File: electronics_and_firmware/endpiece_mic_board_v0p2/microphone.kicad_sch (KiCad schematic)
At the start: 7 parts, among them J1 I2S_MIC_EXT, U1 SPH0645LMH

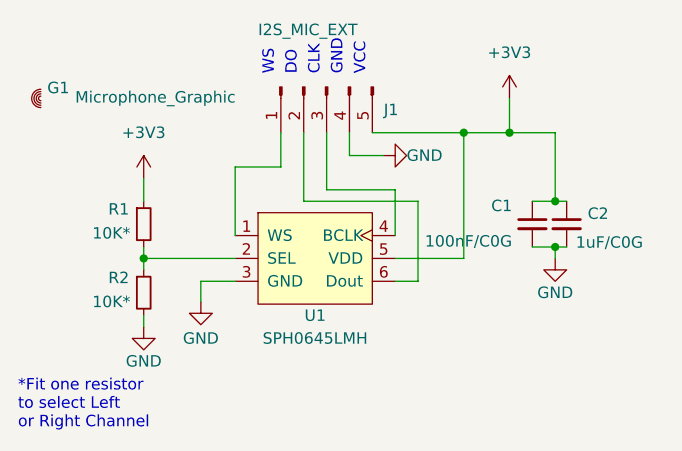
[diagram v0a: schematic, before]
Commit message: change display MOSFET switch to p-type and switch high, thicken some traces on ext. i2s board, slide button down (check this fits capabilities), get rid of via in pad, move i2s line so not over top of psram lines
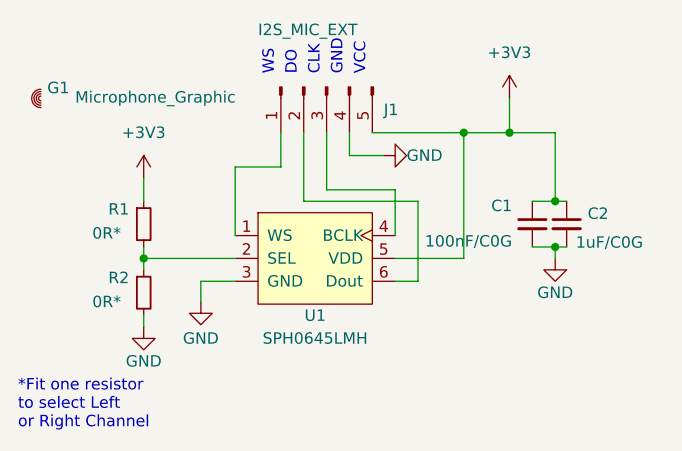
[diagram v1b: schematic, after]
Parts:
- R1, R2: value 10K* -> 0R*
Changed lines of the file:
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@@
       (effects (font (size 1.27 1.27)) (justify left))
     )
-    (property "Value" "10K*" (id 1) (at 137.795 82.296 0)
+    (property "Value" "0R*" (id 1) (at 137.795 82.296 0)
       (effects (font (size 1.27 1.27)) (justify left))
     )
@@
       (effects (font (size 1.27 1.27)) (justify left))
     )
-    (property "Value" "10K*" (id 1) (at 137.795 74.676 0)
+    (property "Value" "0R*" (id 1) (at 137.795 74.676 0)
       (effects (font (size 1.27 1.27)) (justify left))
     )
@@
     )
     (path "/00000000-0000-0000-0000-000062c95f77"
-      (reference "R1") (unit 1) (value "10K*") (footprint "Resistor_SMD:R_0402_1005Metric")
+      (reference "R1") (unit 1) (value "0R*") (footprint "Resistor_SMD:R_0402_1005Metric")
     )
     (path "/00000000-0000-0000-0000-000062c8e0d3"
-      (reference "R2") (unit 1) (value "10K*") (footprint "Resistor_SMD:R_0402_1005Metric")
+      (reference "R2") (unit 1) (value "0R*") (footprint "Resistor_SMD:R_0402_1005Metric")
     )
     (path "/3acedfef-909a-46aa-bd32-28be291ff6fd"
